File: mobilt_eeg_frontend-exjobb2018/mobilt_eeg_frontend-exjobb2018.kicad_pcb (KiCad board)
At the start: 2 copper layers, 95 x 90.5 mm, 126 parts, among them J1 Conn_02x04_Odd_Even, J11 Conn_01x02, J2 Conn_02x20_Odd_Even, J3 Conn_02x04_Odd_Even, J5 Data Header, J8 Conn_01x08, J9 Conn_01x04, P1 Conn_02x20_Odd_Even, SW1 SW_DIP_x01, SW2 SW_DIP_x01, U1 ADS1299-4PAG, U2 TPS60403DBVR, U3 TPS72325DBVT, U4 TPS73225DBVT, U5 TPS73233DBVT, U6 CAT24C256, U7 arduino_pro_mini_3V3_sparkfun, X1 X1G0044810050_SG7050CAN_2.048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

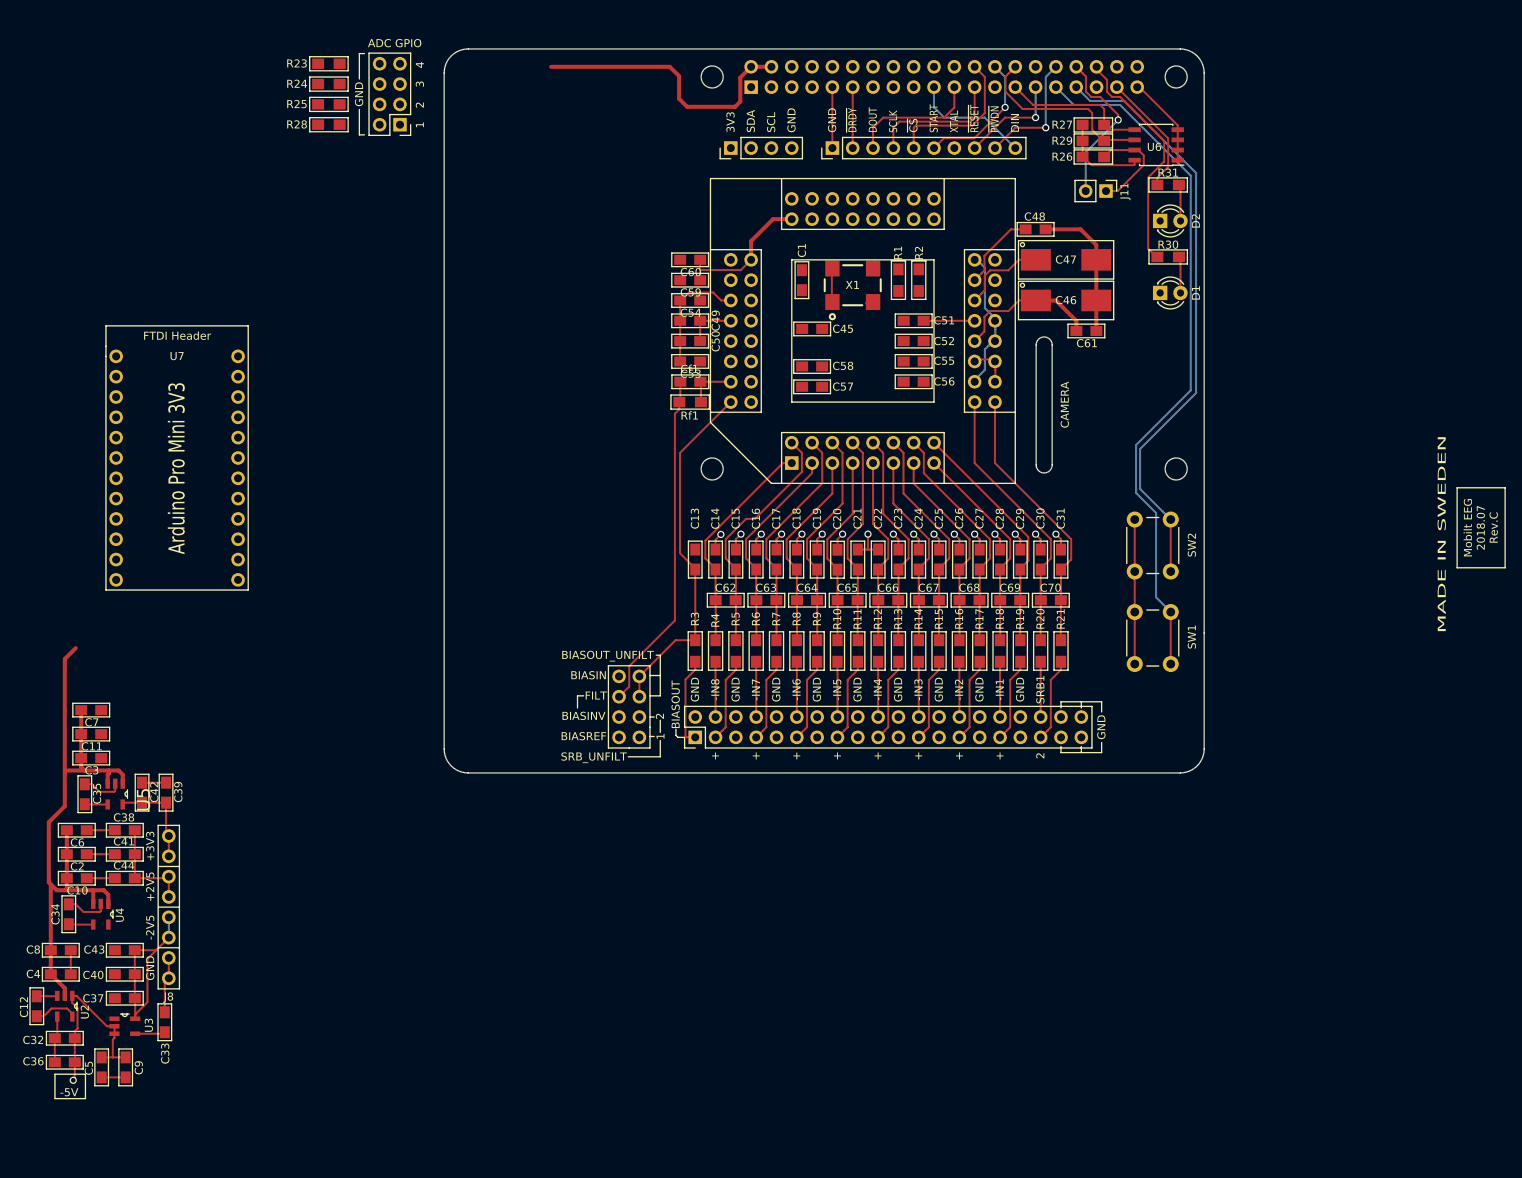
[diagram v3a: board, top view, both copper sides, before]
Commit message: Added a few traces, replaced a remaining GNDD to DGND.
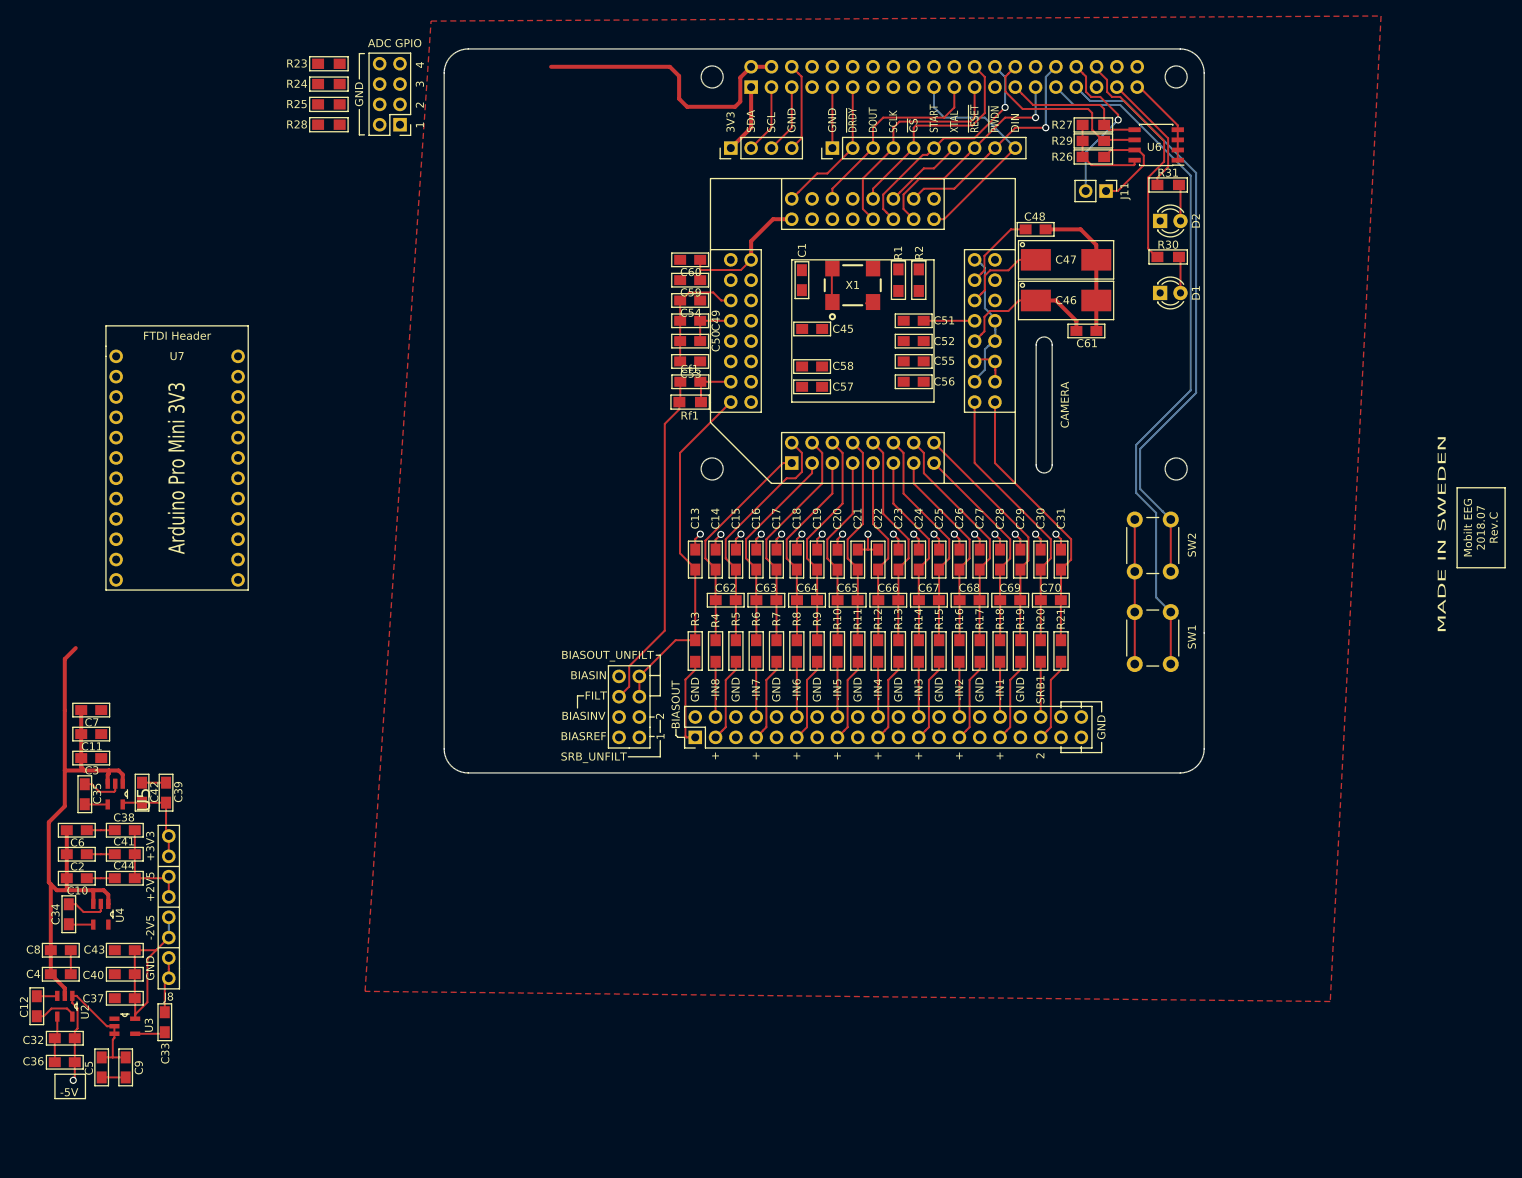
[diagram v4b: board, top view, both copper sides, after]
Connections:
- U1 pad 41: GNDD -> AGND
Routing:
- net /~RESET: track 13.0 -> 27.9 mm
- net /GPIO10(SPI0_MOSI): track 14.8 -> 28.6 mm
- net AGND: track 139.7 -> 153.0 mm, vias 18 -> 19
- net /~PWDN: track 15.5 -> 28.3 mm
- net /START: track 16.6 -> 29.0 mm
- net /GPIO11(SPI0_SCK): track 17.0 -> 28.0 mm
- net /~DRDY: track 7.62 -> 17.9 mm
- net /XTAL: track 0.00 -> 10.3 mm
- net /GPIO3(SCL1): track 0.00 -> 8.67 mm
- net /GPIO2(SDA1): track 0.00 -> 8.67 mm
- net /+3V3_Pi: track 0.00 -> 8.67 mm
- net /GPIO9(SPI0_MISO): track 16.3 -> 24.7 mm
- net /GPIO8(SPI0_CE_N): track 18.5 -> 27.0 mm
- added copper zone on F.Cu, net AGND

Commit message: savea nu baa
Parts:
- moved C39 80.2 mm to (193.4, 131.8), turned to 270 degrees
- moved C42 80.2 mm to (190.4, 131.8), turned to 270 degrees
- moved C35 80.0 mm to (186.4, 135.8), turned to 0 degrees
- moved U5 79.8 mm to (186.4, 131.8)
- moved C7 72.1 mm to (182.4, 131.8), turned to 270 degrees
- moved C11 71.8 mm to (179.4, 131.8), turned to 270 degrees
- moved C3 71.7 mm to (176.4, 131.8), turned to 270 degrees
- moved U7 59.4 mm to (177.9, 98.8)
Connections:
- U7 pad 21: Net-(U7-Pad21) -> +5V
- U7 pad 4: Net-(U7-Pad4) -> AGND
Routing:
- net +5V: track 117.5 -> 181.9 mm
- net AGND: track 153.0 -> 172.8 mm
- net AVSS: track 75.8 -> 95.0 mm, vias 0 -> 1
- net DVDD: track 45.9 -> 61.3 mm
- net AVDD: track 18.0 -> 29.4 mm
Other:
- board text added: "SMD components: try to go for 1mm spacing."

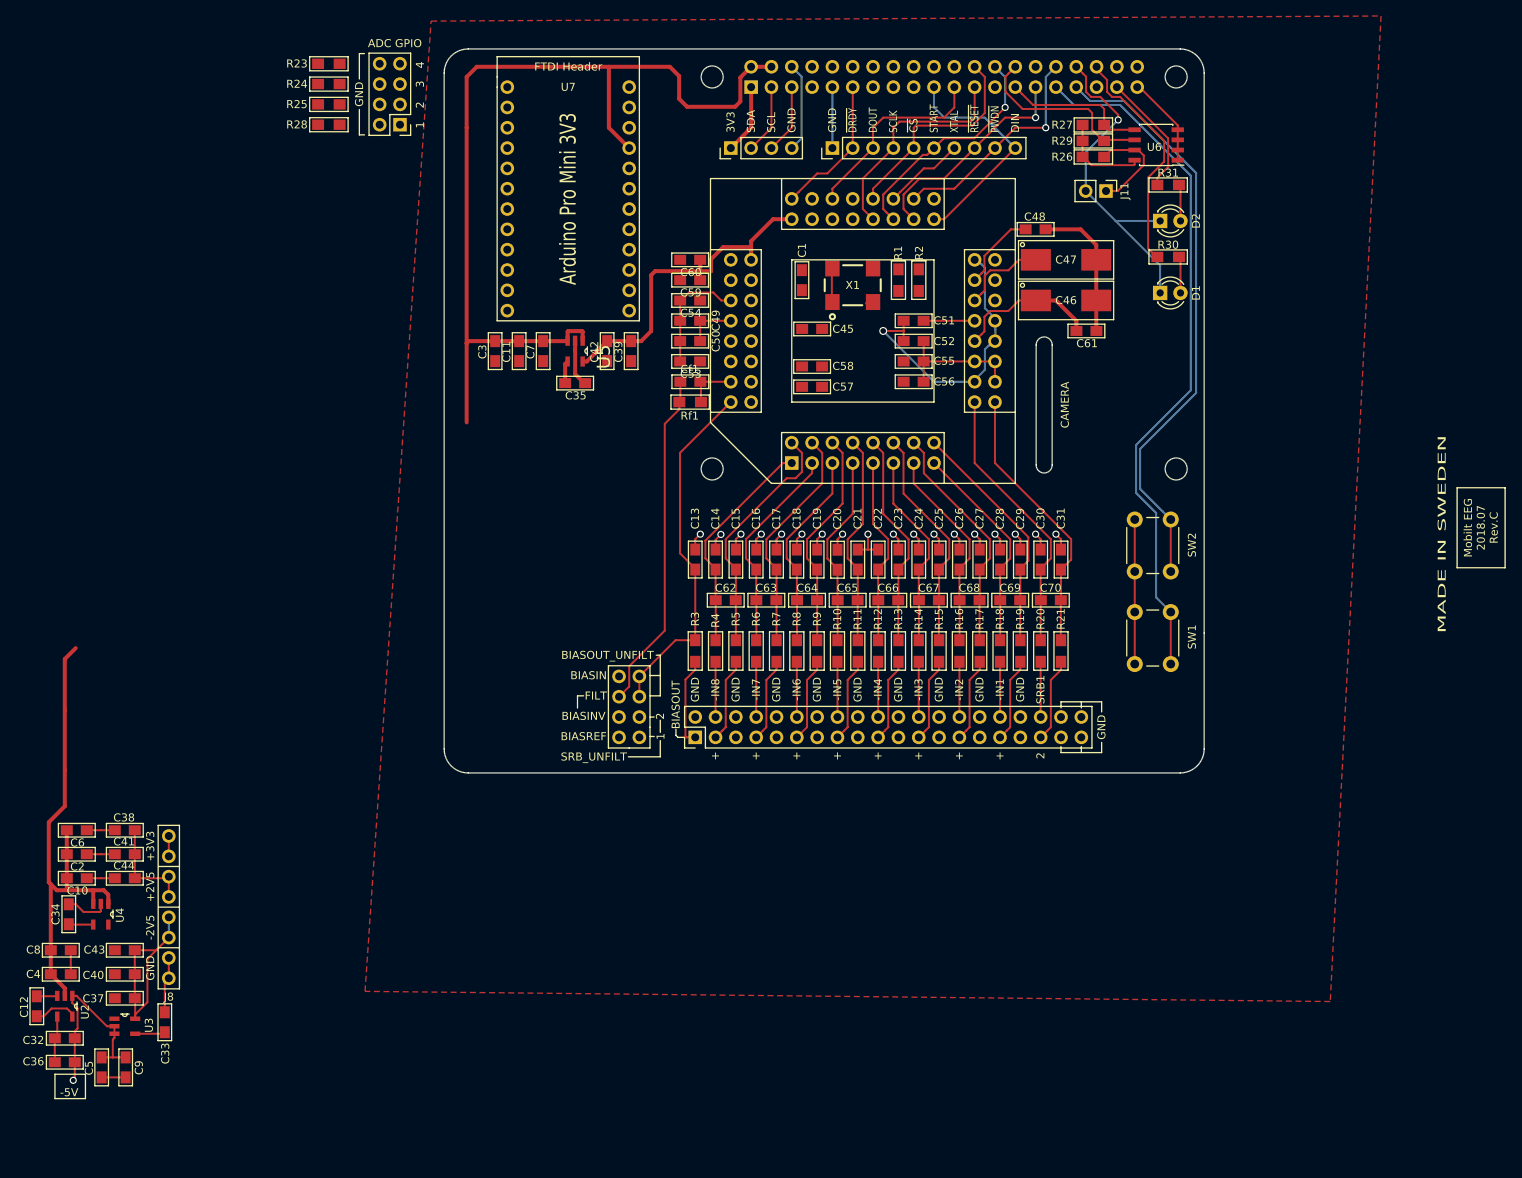
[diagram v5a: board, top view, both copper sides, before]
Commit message: Aligned PSU sections in individual "columns" and aligned to 1mm grid .
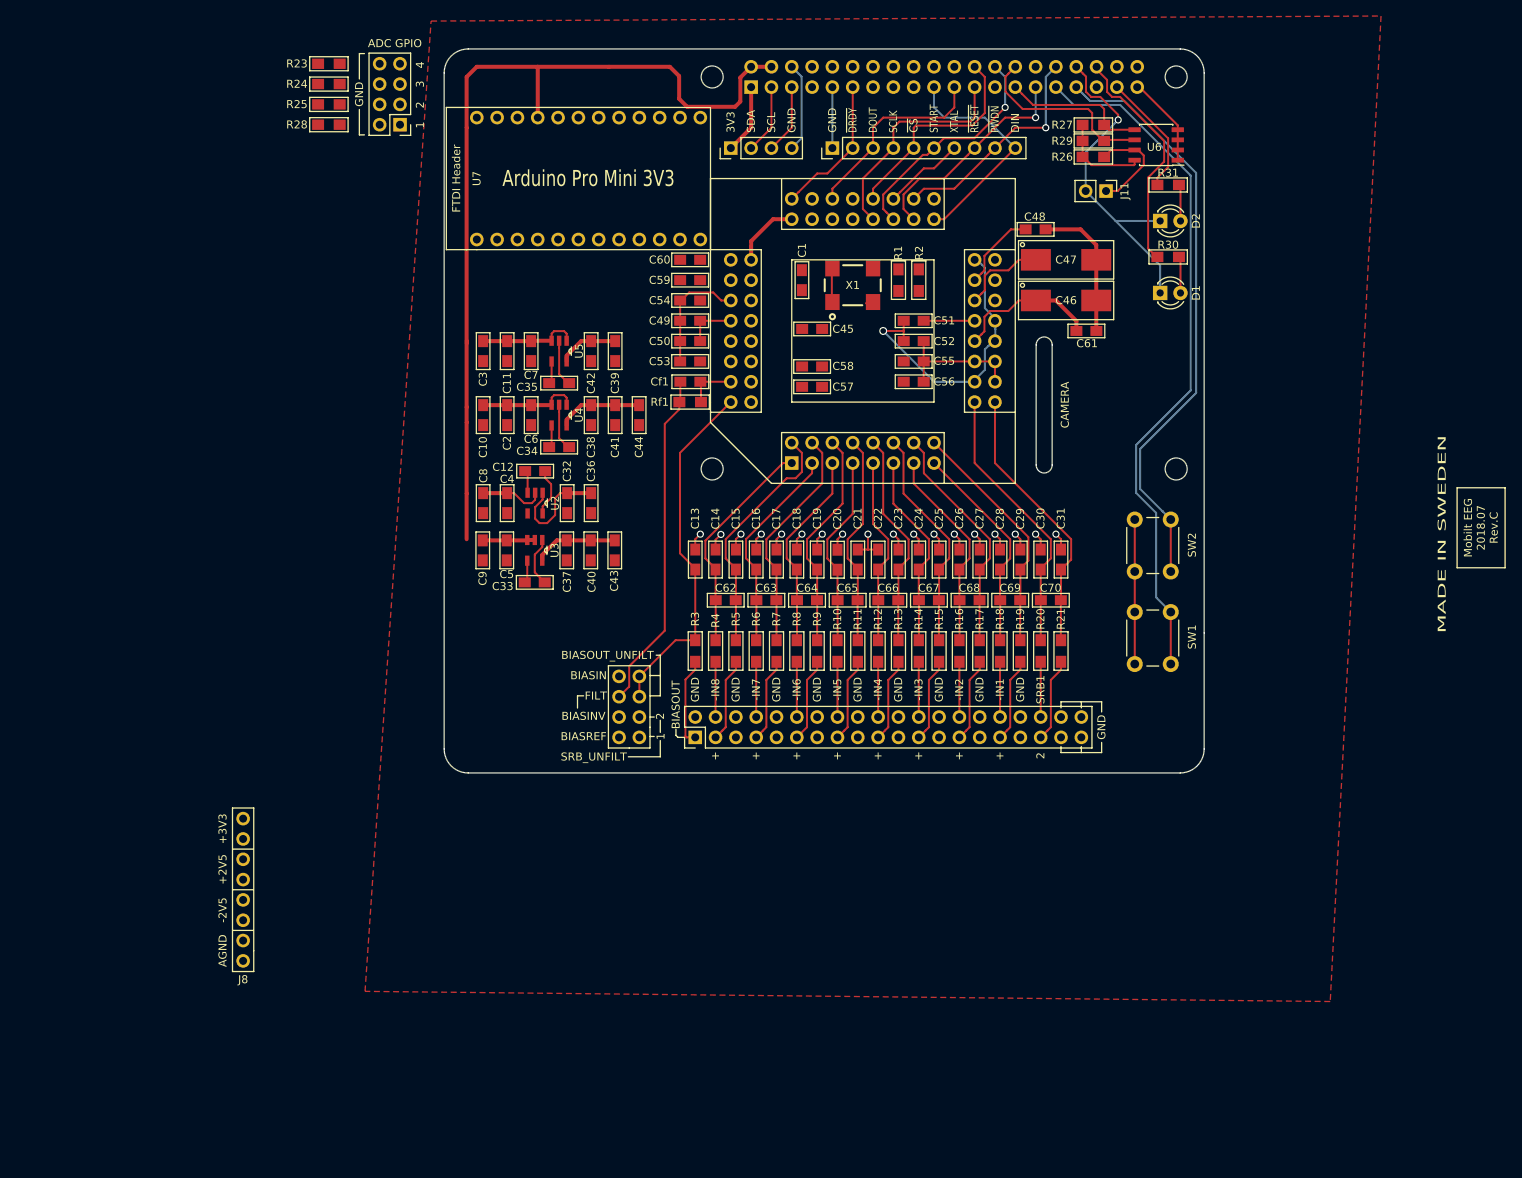
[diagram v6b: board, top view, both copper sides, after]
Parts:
- moved C36 96.0 mm to (188.4, 150.8), turned to 270 degrees
- moved C32 91.7 mm to (185.4, 150.8), turned to 270 degrees
- moved C12 91.4 mm to (181.4, 146.8), turned to 0 degrees
- moved C44 86.5 mm to (194.4, 139.8), turned to 270 degrees
- moved U2 86.1 mm to (181.4, 150.8)
- moved U4 84.7 mm to (184.4, 139.8)
- moved C34 84.7 mm to (184.4, 143.8), turned to 0 degrees
- moved C41 82.3 mm to (191.4, 139.8), turned to 270 degrees
- moved C5 82.1 mm to (177.8, 156.7)
- moved C4 81.1 mm to (177.9, 150.8), turned to 270 degrees
- moved C43 79.1 mm to (191.3, 156.7), turned to 270 degrees
- moved C40 78.7 mm to (188.3, 156.7), turned to 270 degrees
- moved C37 78.7 mm to (185.3, 156.7), turned to 270 degrees
- moved C9 78.5 mm to (174.8, 156.7)
- moved U3 78.5 mm to (181.3, 156.7), turned to 270 degrees
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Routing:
- net +5V: track 181.9 -> 143.4 mm
- net DVDD: track 61.3 -> 31.6 mm
- net AGND: track 172.8 -> 150.3 mm
- net AVSS: track 95.0 -> 79.7 mm
- net /-5V_unreg: track 24.9 -> 20.2 mm, vias 1 -> 0
- net AVDD: track 29.4 -> 27.1 mm
- net Net-(C33-Pad1): track 3.78 -> 2.83 mm
- net Net-(C12-Pad2): track 5.47 -> 6.05 mm
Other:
- board text added: "AGND"
- board text added: "Min character width: 5mil [0.15] Min character height: 32mil [0.8]"
- board text removed: "-5V"

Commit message: stuffelistuff
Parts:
- U2, U3, U4, U5: footprint SOT95P280X145-5N -> TPS73233DBVT:SOT95P280X145-5N
- moved C10 52.8 mm to (122.8, 130.9)
- moved C11 52.8 mm to (125.8, 122.9)
- moved C2 52.8 mm to (125.8, 130.9)
- moved C3 52.8 mm to (122.8, 122.9)
- moved C4 52.8 mm to (125.8, 141.9)
- moved C8 52.8 mm to (122.8, 141.9)
- moved C12 52.8 mm to (129.3, 137.9)
- moved C32 52.8 mm to (133.3, 141.9)
- moved C33 52.8 mm to (129.3, 151.8)
- moved C34 52.8 mm to (132.3, 134.9)
- moved C35 52.8 mm to (132.3, 126.9)
- moved C36 52.8 mm to (136.3, 141.9)
- moved C37 52.8 mm to (133.3, 147.8)
- moved C38 52.8 mm to (136.3, 130.9)
- moved C39 52.8 mm to (139.3, 122.9)
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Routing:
- net +5V: track 143.4 -> 76.2 mm
- net AGND: track 150.3 -> 104.4 mm, vias 19 -> 18
- net DVDD: track 31.6 -> 49.2 mm
- net /GPIO6: track 87.1 -> 75.0 mm, vias 0 -> 1
- net AVDD: track 27.1 -> 38.3 mm
- net /XTAL: track 10.3 -> 20.7 mm
- net /GPIO13(PWM1): track 73.7 -> 68.4 mm
- net Net-(J11-Pad1): track 12.9 -> 8.08 mm
- net /ID_SD: track 18.9 -> 14.2 mm
- net /ID_SC: track 23.6 -> 20.1 mm
- net AVSS: track 79.7 -> 76.3 mm, vias 1 -> 0
- net /GPIO26: track 15.4 -> 14.5 mm
- net /~PWDN: track 28.3 -> 27.6 mm
- net Net-(D2-Pad2): track 4.58 -> 3.84 mm
- net Net-(D1-Pad2): track 4.58 -> 3.84 mm
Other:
- board text added: "LEDs use 2.54mm grid!"

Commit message: savea
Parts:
- U2, U3, U4, U5: footprint TPS73233DBVT:SOT95P280X145-5N -> SOT95P280X145-5N
- moved U7 19.1 mm to (172.8, 98.8), turned to 0 degrees
- moved C39 3.07 mm to (142.4, 122.8)
- moved C42 3.07 mm to (139.4, 122.8)
- moved R1 1.00 mm to (228.4, 121.8)
- moved R2 1.00 mm to (231.4, 121.8)
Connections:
- U7 pad 21: +5V -> DVDD
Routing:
- net /BIASIN: track 0.00 -> 45.2 mm
- net +5V: track 76.2 -> 33.1 mm
- net AGND: track 104.4 -> 147.1 mm
- net /~PWDN: track 27.6 -> 36.4 mm
- net /~RESET: track 27.9 -> 33.2 mm
- net DVDD: track 49.2 -> 46.2 mm
- net Net-(Cf1-Pad2): track 42.5 -> 43.6 mm
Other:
- board text added: "ALT PCB 1"
- board text removed: "GRID OVERHAUL"
